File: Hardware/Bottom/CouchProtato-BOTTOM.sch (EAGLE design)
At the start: 32 parts, among them U1 AD5242-SO16

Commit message: Progress on routing bottom board and schematic
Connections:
- removed net LED: Q1.C
- net 3.3V: now also J1.4
- net GND: now also J1.3
- net LED.C: now also Q1.C
- net SCL: now also J1.2
- net SDA: now also J1.1
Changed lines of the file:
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@@
 <part name="SUPPLY24" library="LinnesLab-Symbols" deviceset="3.3V" device=""/>
 <part name="J1" library="LinnesLab-Connectors" deviceset="CONN_07" device=""/>
+<part name="GND1" library="LinnesLab-Symbols" deviceset="GND" device=""/>
+<part name="SUPPLY1" library="LinnesLab-Symbols" deviceset="3.3V" device=""/>
 </parts>
 <sheets>
@@
 <attribute name="NAME" x="93.98" y="-37.592" size="1.778" layer="95" font="vector"/>
 </instance>
+<instance part="GND1" gate="G$1" x="106.68" y="-63.5" smashed="yes">
+<attribute name="VALUE" x="106.68" y="-63.754" size="1.778" layer="96" align="top-center"/>
+</instance>
+<instance part="SUPPLY1" gate="G$1" x="106.68" y="-35.56" smashed="yes">
+<attribute name="VALUE" x="106.68" y="-32.766" size="1.778" layer="96" align="bottom-center"/>
+</instance>
 </instances>
 <busses>
@@
 <wire x1="0" y1="-58.42" x2="0" y2="-55.88" width="0.1524" layer="91"/>
 </segment>
+<segment>
+<pinref part="J1" gate="G$1" pin="3"/>
+<wire x1="104.14" y1="-50.8" x2="106.68" y2="-50.8" width="0.1524" layer="91"/>
+<pinref part="GND1" gate="G$1" pin="GND"/>
+<wire x1="106.68" y1="-60.96" x2="106.68" y2="-50.8" width="0.1524" layer="91"/>
+</segment>
 </net>
 <net name="3.3V" class="0">
@@
 <wire x1="0" y1="-45.72" x2="0" y2="-48.26" width="0.1524" layer="91"/>
 </segment>
+<segment>
+<pinref part="J1" gate="G$1" pin="4"/>
+<wire x1="104.14" y1="-48.26" x2="106.68" y2="-48.26" width="0.1524" layer="91"/>
+<pinref part="SUPPLY1" gate="G$1" pin="3.3V"/>
+<wire x1="106.68" y1="-35.56" x2="106.68" y2="-48.26" width="0.1524" layer="91"/>
+</segment>
 </net>
 <net name="SDA" class="0">
@@
 <label x="40.64" y="-50.8" size="1.27" layer="95" xref="yes"/>
 </segment>
+<segment>
+<pinref part="J1" gate="G$1" pin="1"/>
+<wire x1="104.14" y1="-55.88" x2="106.68" y2="-55.88" width="0.1524" layer="91"/>
+<label x="106.68" y="-55.88" size="1.27" layer="95" xref="yes"/>
+</segment>
 </net>
 <net name="SCL" class="0">
@@
 <wire x1="38.1" y1="-55.88" x2="40.64" y2="-55.88" width="0.1524" layer="91"/>
 <label x="40.64" y="-55.88" size="1.27" layer="95" xref="yes"/>
+</segment>
+<segment>
+<pinref part="J1" gate="G$1" pin="2"/>
+<wire x1="104.14" y1="-53.34" x2="106.68" y2="-53.34" width="0.1524" layer="91"/>
+<label x="106.68" y="-53.34" size="1.27" layer="95" xref="yes"/>
 </segment>
 </net>
@@
 <label x="27.94" y="88.9" size="1.27" layer="95" xref="yes"/>
 </segment>
+<segment>
+<wire x1="233.68" y1="2.54" x2="233.68" y2="5.08" width="0.1524" layer="91"/>
+<label x="233.68" y="5.08" size="1.27" layer="95" rot="R180" xref="yes"/>
+<pinref part="Q1" gate="G$1" pin="C"/>
+</segment>
 </net>
 <net name="VREF" class="0">
@@
 </segment>
 </net>
-<net name="LED" class="0">
-<segment>
-<wire x1="233.68" y1="2.54" x2="233.68" y2="5.08" width="0.1524" layer="91"/>
-<label x="233.68" y="5.08" size="1.27" layer="95" rot="R180" xref="yes"/>
-<pinref part="Q1" gate="G$1" pin="C"/>
-</segment>
-</net>

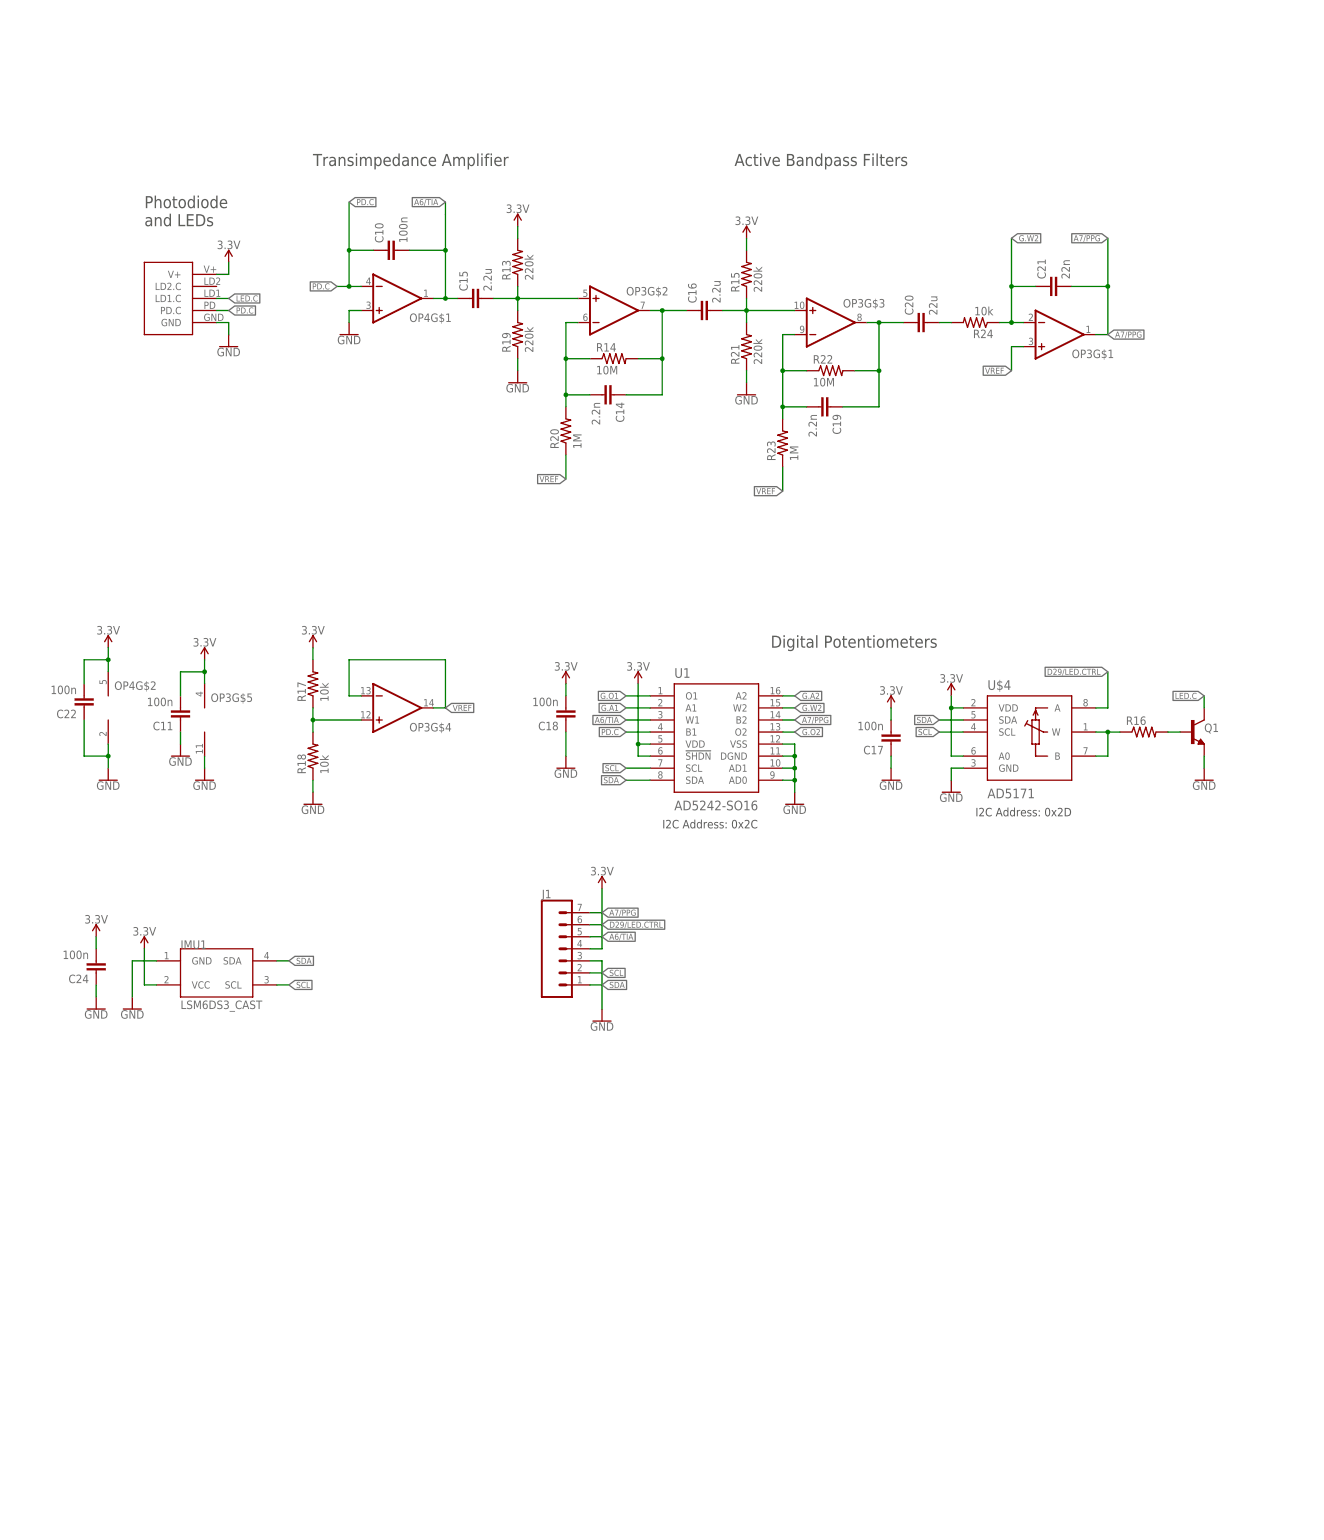
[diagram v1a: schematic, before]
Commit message: finished routing bottom board and began top. finished take 003.
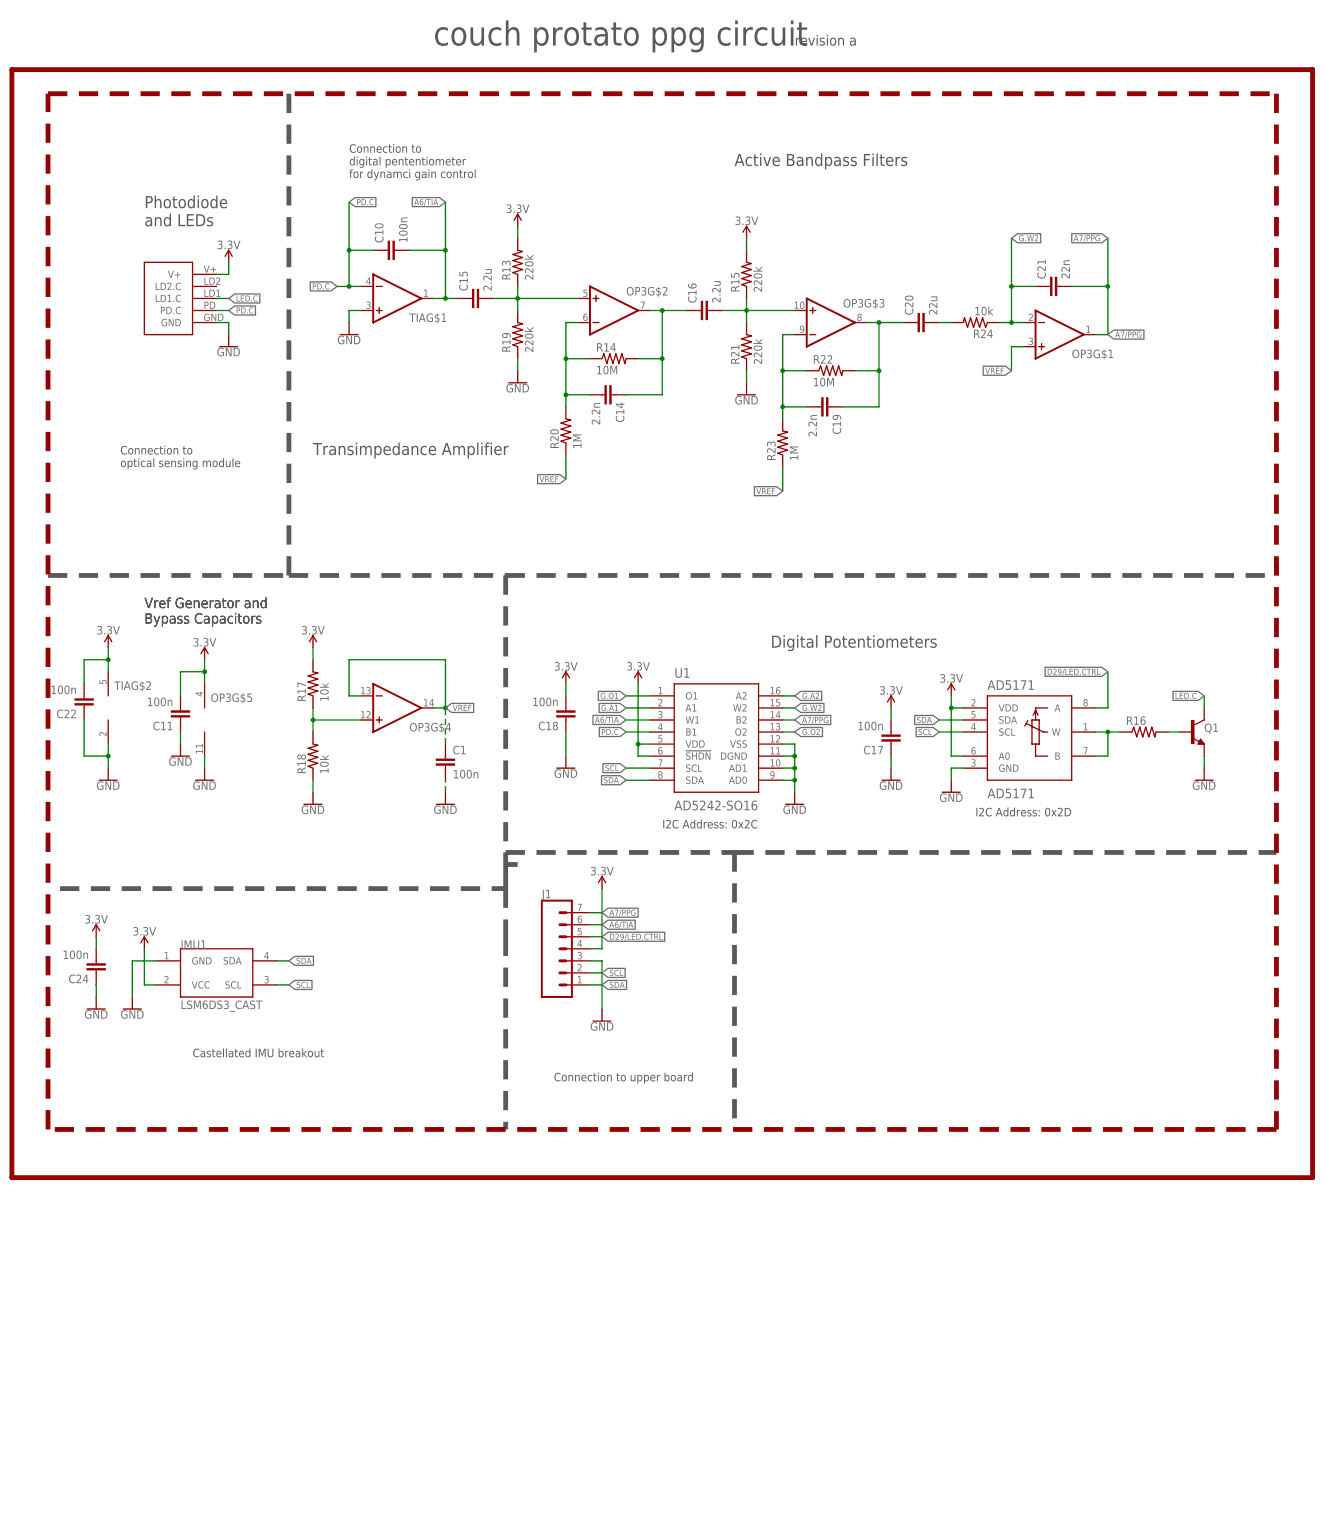
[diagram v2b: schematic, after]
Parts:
- added C1: 100n, LinnesLab-Passives:CAPACITOR0603
- J1: device LinnesLab-Connectors:CONN_07 -> LinnesLab-Connectors:CONN_07-1.27MM
- renumbered OP4 to TIA, U$4 to AD5171
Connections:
- net A6/TIA: now also J1.6; no longer J1.5
- net D29/LED.CTRL: now also J1.5; no longer J1.6
- net GND: now also C1.2
- net VREF: now also C1.1
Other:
- note added: "Castellated IMU breakout"
- note added: "Connection to digital pententiometer for dynamci gain control"
- note added: "Connection to optical sensing module"
- note added: "Connection to upper board"
- note added: "Vref Generator and Bypass Capacitors"
- note added: "couch protato ppg circuit"
- note added: "revision a"

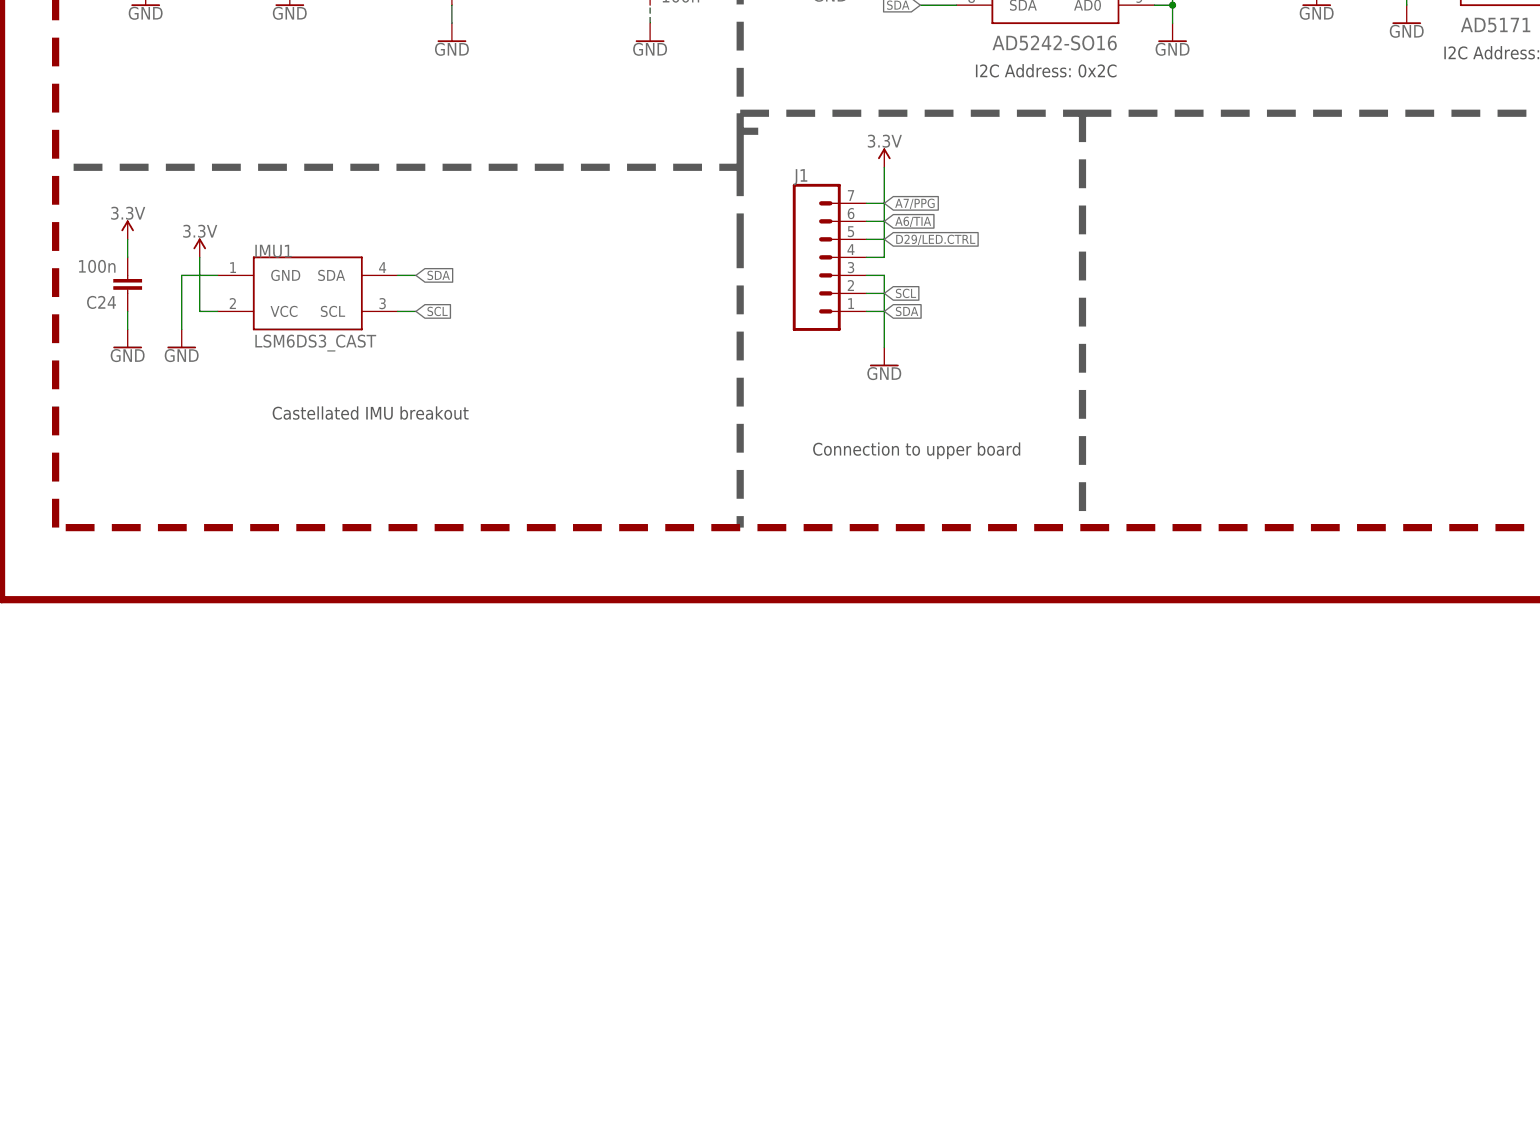
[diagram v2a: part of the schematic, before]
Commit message: Finished take 7, one more how to video to go, reorganizing and finalizing boards
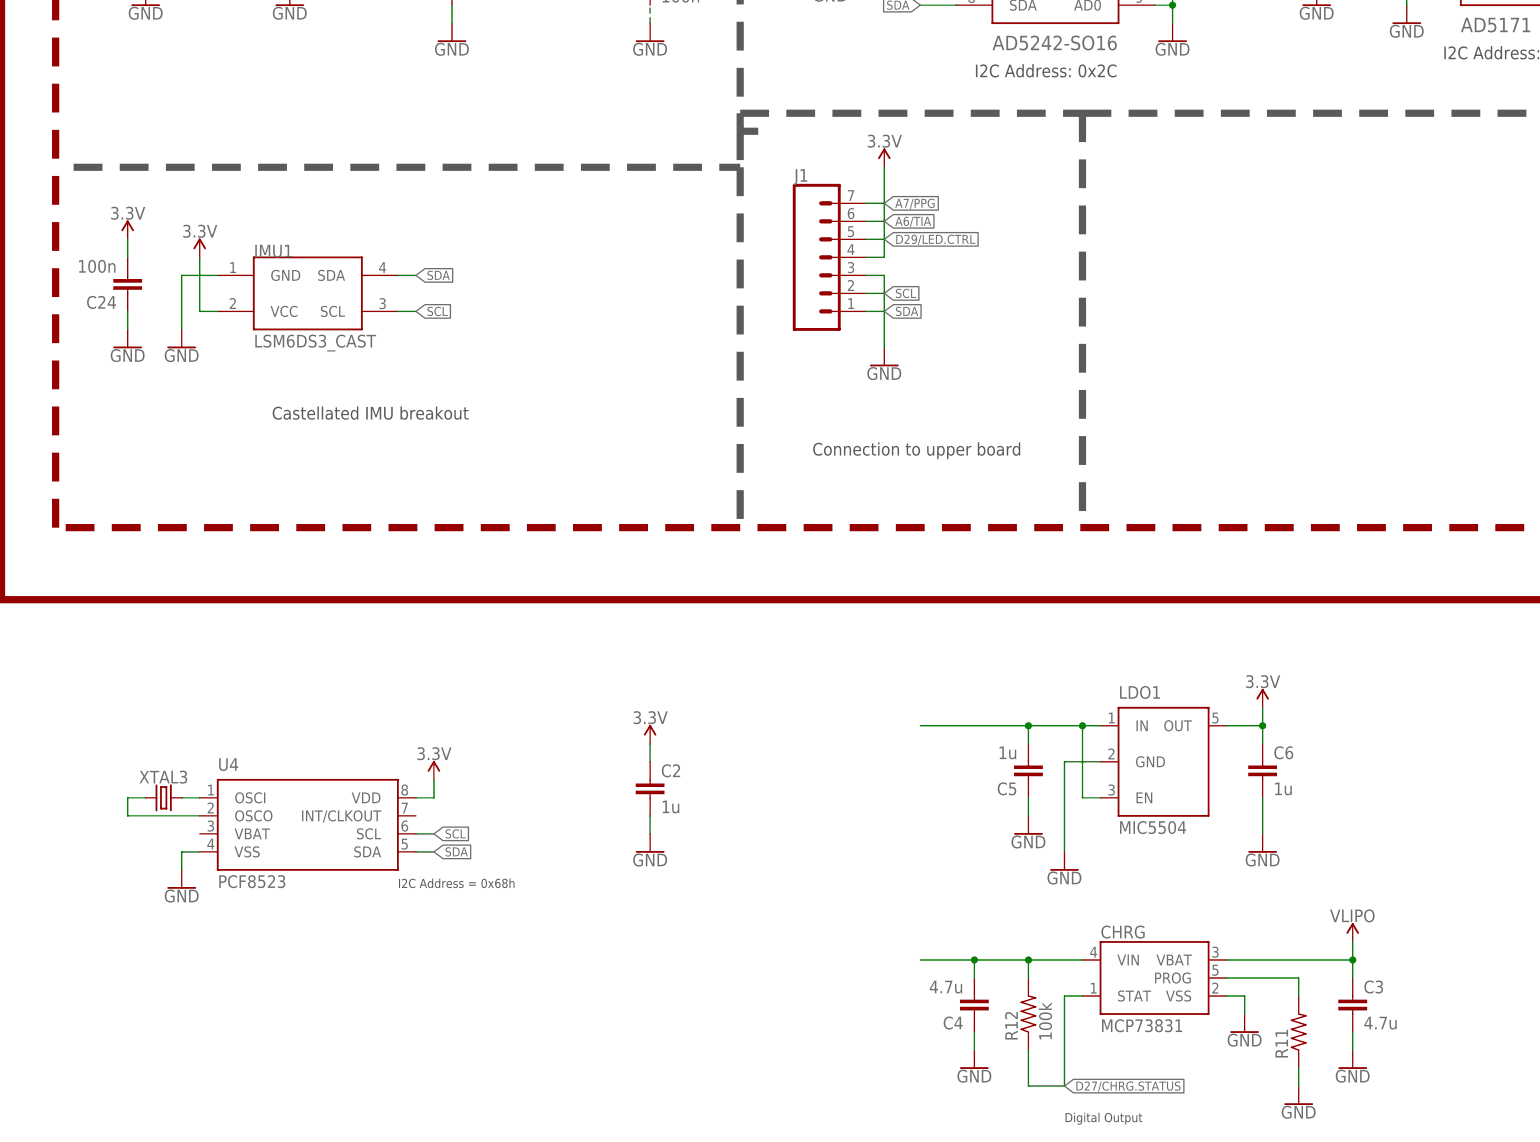
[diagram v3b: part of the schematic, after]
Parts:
- added C2, C5, C6: 1u, LinnesLab-Passives:CAPACITOR0603
- added C3, C4: 4.7u, LinnesLab-Passives:CAPACITOR0603
- added CHRG: MCP73831, LinnesLab-Power:MCP73831
- added LDO1: MIC5504, LinnesLab-Power:MIC5504
- added R11: (no value), LinnesLab-Passives:RESISTOR0603
- added R12: 100k, LinnesLab-Passives:RESISTOR0603
- added U4: PCF8523, LinnesLab-Clocks:PCF8523
- added XTAL3: 32.7680kHz, LinnesLab-Clocks:CRYSTALECS-.327-12.5-12-C-TR
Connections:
- new net D27/CHRG.STATUS: CHRG.STAT, R12.1
- new net N$1: U4.OSCO, XTAL3.1
- new net N$2: U4.OSCI, XTAL3.2
- new net N$3: CHRG.PROG, R11.2
- new net VIN1: C4.2, C5.2, CHRG.VIN, LDO1.EN, LDO1.IN, R12.2
- new net VLIPO: C3.1, CHRG.VBAT
- net 3.3V: now also C2.1, C6.1, LDO1.OUT, U4.VDD
- net GND: now also C2.2, C3.2, C4.1, C5.1, C6.2, CHRG.VSS, LDO1.GND, R11.1, U4.VSS
- net SCL: now also U4.SCL
- net SDA: now also U4.SDA
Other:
- note added: "Digital Output"
- note added: "I2C Address = 0x68h"
